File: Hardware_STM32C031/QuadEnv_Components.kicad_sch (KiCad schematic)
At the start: 50 parts, among them J1 Eurorack_10_pin_power, J2 Conn_01x04_Male, J3 Conn_01x04_Male, J4 Conn_01x04_Male, J5 Conn_01x04_Male, U1 STM32C031C6T, U2 LD1117-3.3-4Tab, U3 TL074

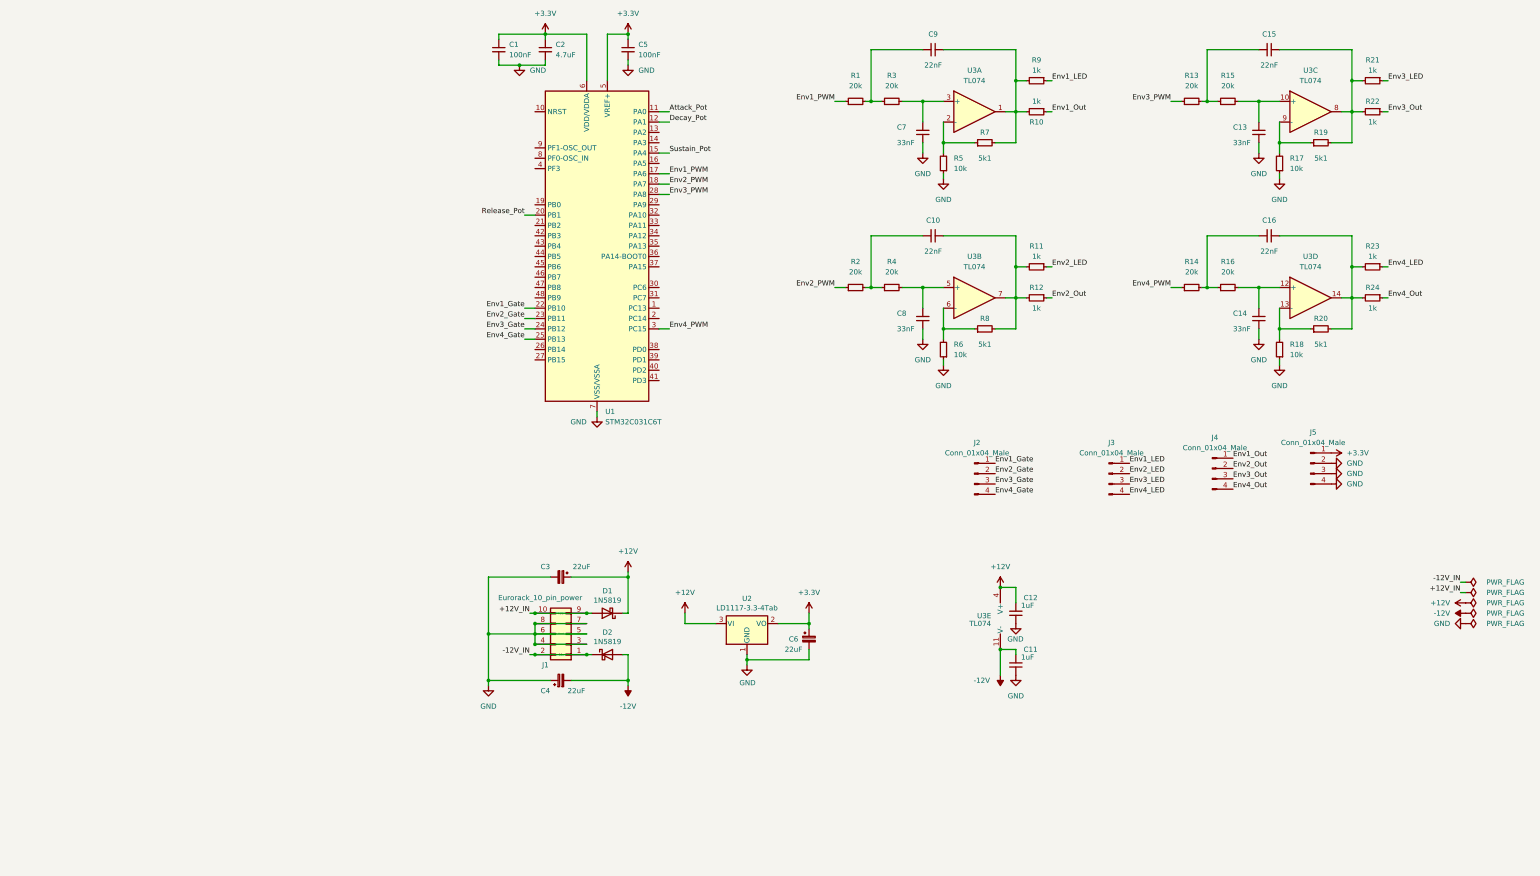
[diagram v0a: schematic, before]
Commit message: Completed first draft of components PCB
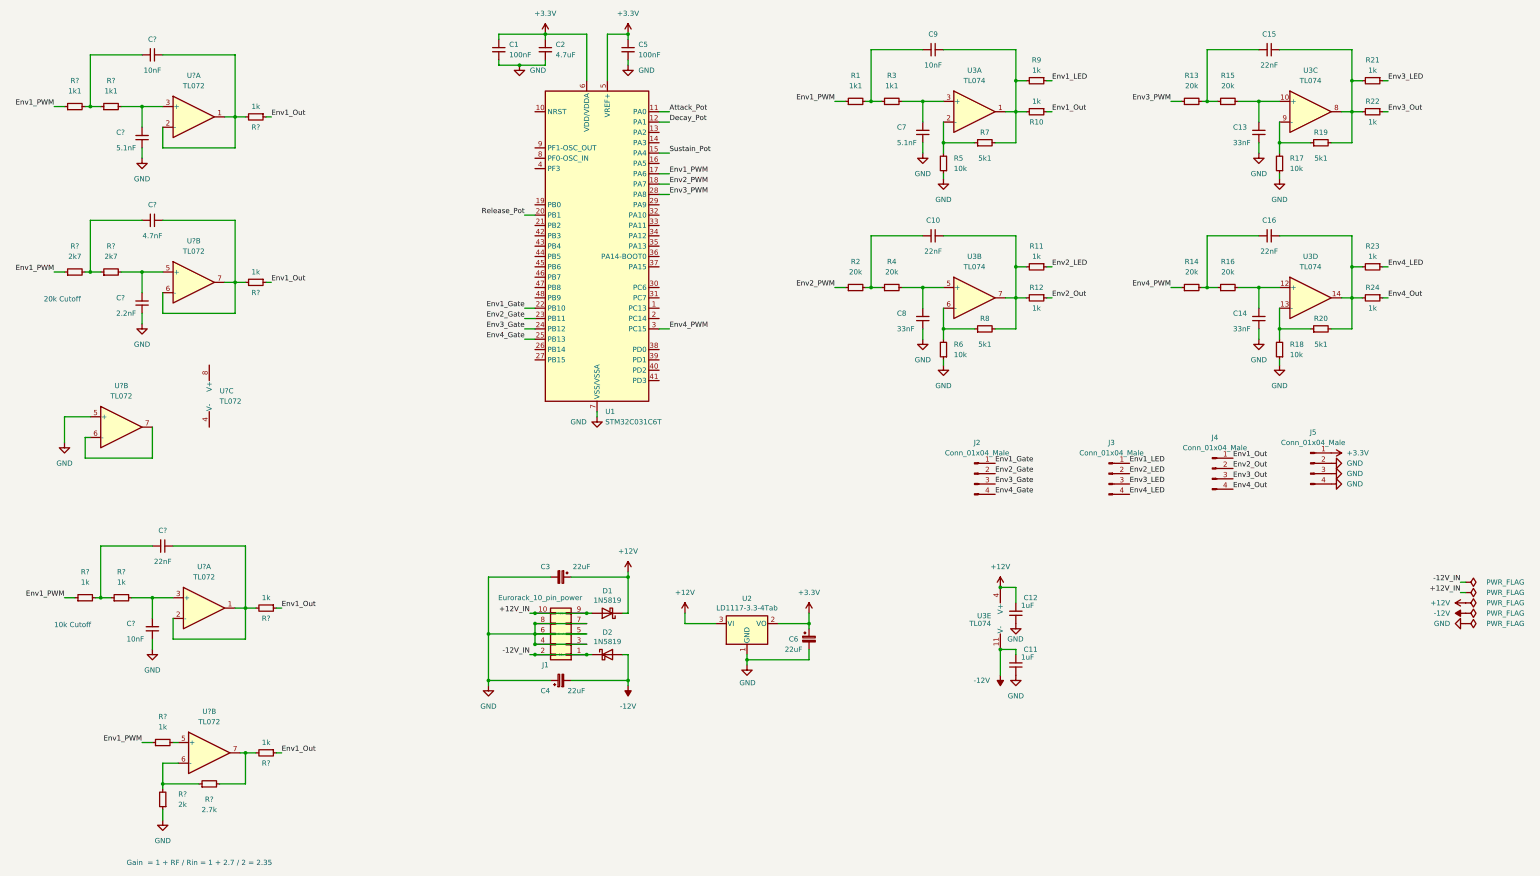
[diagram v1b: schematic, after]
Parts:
- added C? (x2): 10nF, Capacitor_SMD:C_0603_1608Metric, symbol Device:C_Small
- added C?: 2.2nF, Capacitor_SMD:C_0603_1608Metric, symbol Device:C_Small
- added C?: 4.7nF, Capacitor_SMD:C_0603_1608Metric, symbol Device:C_Small
- added C?: 5.1nF, Capacitor_SMD:C_0603_1608Metric, symbol Device:C_Small
- added C?: 22nF, Capacitor_SMD:C_0603_1608Metric, symbol Device:C_Small
- added R? (x7): 1k, Resistor_SMD:R_0603_1608Metric, symbol Device:R_Small
- added R? (x2): 1k1, Resistor_SMD:R_0603_1608Metric, symbol Device:R_Small
- added R? (x2): 2k7, Resistor_SMD:R_0603_1608Metric, symbol Device:R_Small
- added R?: 2k, Resistor_SMD:R_0603_1608Metric, symbol Device:R_Small
- added R?: 2.7k, Resistor_SMD:R_0603_1608Metric, symbol Device:R_Small
- added U? (x6): TL072, symbol Amplifier_Operational:TL072
- C7: value 33nF -> 5.1nF
- C9: value 22nF -> 10nF
- R1, R3: value 20k -> 1k1
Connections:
- net Env1_Out: now also R?.1, R?.1, R?.1, R?.1
- net Env1_PWM: now also R?.1, R?.1, R?.1, R?.1
- net GND: now also C?.1, C?.1, C?.1, R?.1, U?.5 (+)
- new net: U?.6 (-), U?.7
- new net: R?.2, R?.2, U?.7
- new net: C?.2, R?.2, U?.3 (+) (x2)
- new net: C?.1, R?.2, U?.1, U?.2 (-) (x2)
- new net: C?.2, R?.1, R?.2 (x3)
- new net: R?.2, U?.5 (+)
- new net: C?.1, R?.2, U?.6 (-), U?.7
- new net: C?.2, R?.2, U?.5 (+)
- new net: R?.1, R?.2, U?.6 (-)
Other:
- note added: "10k Cutoff"
- note added: "20k Cutoff"
- note added: "Gain = 1 + RF / Rin = 1 + 2.7 / 2 = 2.35"
